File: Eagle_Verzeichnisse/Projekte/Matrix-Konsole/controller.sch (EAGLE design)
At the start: 14 parts, among them IC1 74HC165D, X2 MINI-USB-32005-201

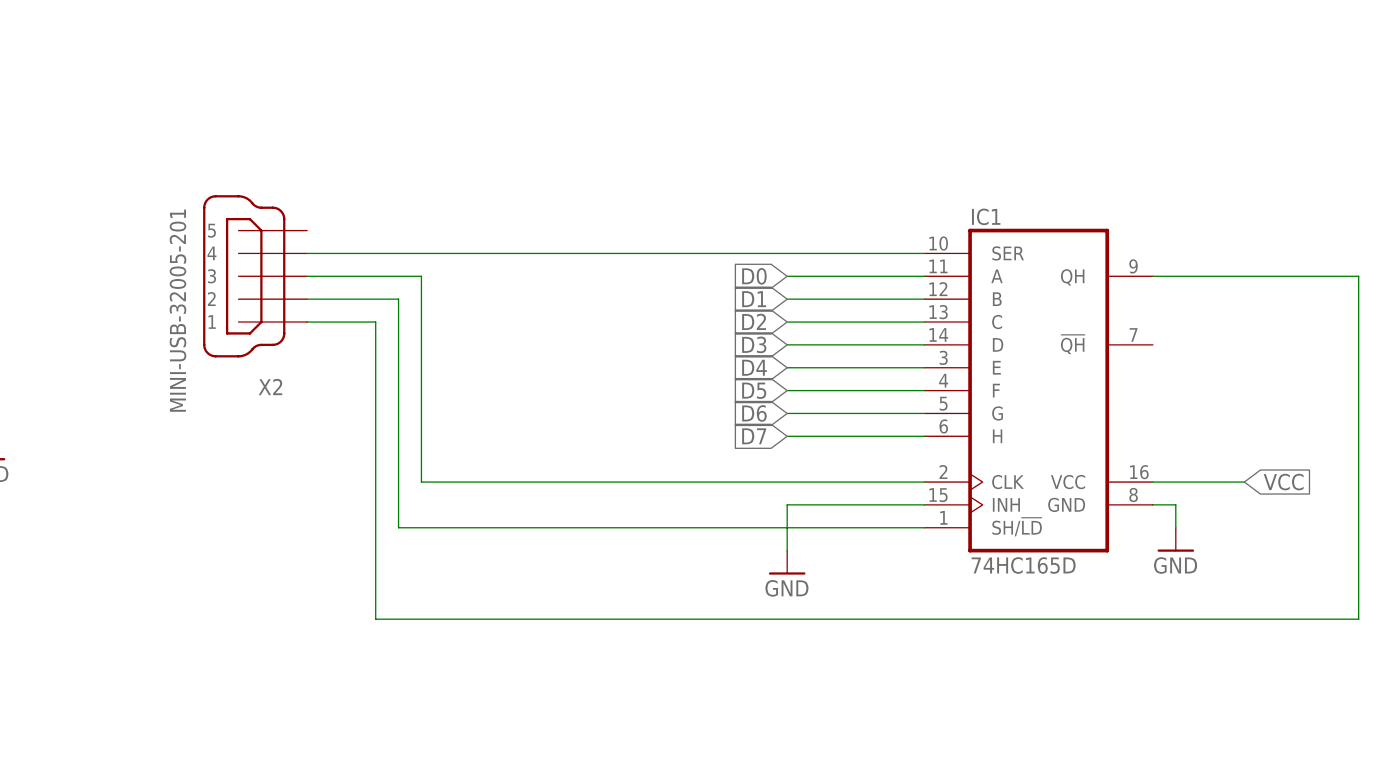
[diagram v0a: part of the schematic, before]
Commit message: Removed USB, Changed Labels
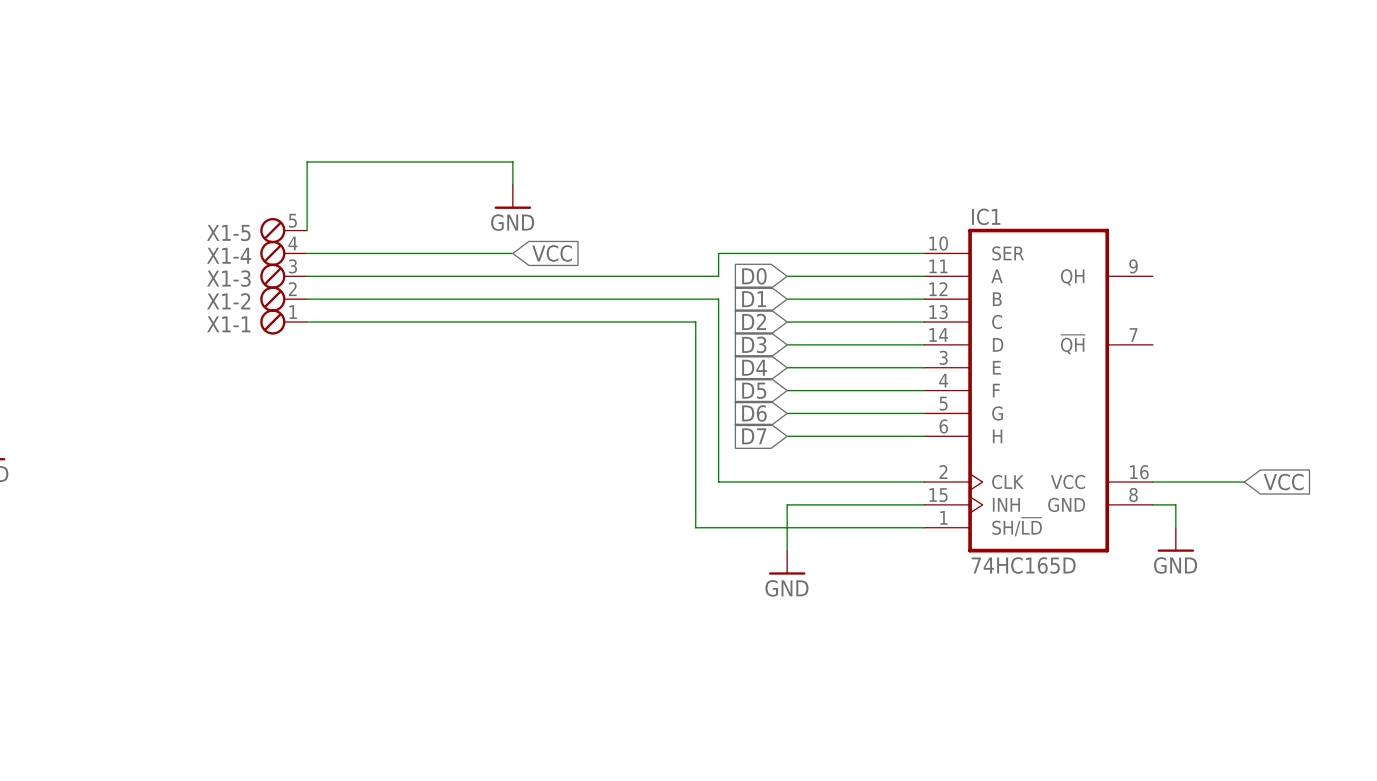
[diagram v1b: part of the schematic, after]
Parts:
- removed X2: MINI-USB-32005-201, con-cypressindustries:MINI-USB-32005-201
- added X1: (no value), con-phoenix-254:MPT5
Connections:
- removed net N$4: IC1.QH, X2.1
- net GND: now also X1-5.1
- net N$1: now also IC1.SH/!LD, X1-1.1; no longer IC1.SER, X2.4
- net N$2: now also X1-2.1; no longer X2.3
- net N$3: now also IC1.SER, X1-3.1; no longer IC1.SH/!LD, X2.2
- net VCC: now also X1-4.1
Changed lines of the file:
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@@
 <setting verticaltext="up"/>
 </settings>
-<grid distance="0.1" unitdist="inch" unit="inch" style="lines" multiple="1" display="no" altdistance="0.01" altunitdist="inch" altunit="inch"/>
+<grid distance="0.1" unitdist="inch" unit="inch" style="lines" multiple="1" display="yes" altdistance="0.01" altunitdist="inch" altunit="inch"/>
 <layers>
 <layer number="1" name="Top" color="4" fill="1" visible="no" active="no"/>
@@
 <part name="GND7" library="supply1" deviceset="GND" device=""/>
 <part name="GND8" library="supply1" deviceset="GND" device=""/>
-<part name="X2" library="con-cypressindustries" deviceset="MINI-USB-" device="32005-201"/>
+<part name="X1" library="con-phoenix-254" deviceset="MPT5" device=""/>
+<part name="GND9" library="supply1" deviceset="GND" device=""/>
 </parts>
 <sheets>
@@
 <instance part="GND7" gate="1" x="-86.36" y="-50.8"/>
 <instance part="GND8" gate="1" x="-5.08" y="22.86"/>
-<instance part="X2" gate="G$1" x="-63.5" y="55.88" rot="R180"/>
+<instance part="X1" gate="-1" x="-60.96" y="50.8" rot="R180"/>
+<instance part="X1" gate="-2" x="-60.96" y="53.34" rot="R180"/>
+<instance part="X1" gate="-3" x="-60.96" y="55.88" rot="R180"/>
+<instance part="X1" gate="-4" x="-60.96" y="58.42" rot="R180"/>
+<instance part="X1" gate="-5" x="-60.96" y="60.96" rot="R180"/>
+<instance part="GND9" gate="1" x="-35.56" y="63.5"/>
 </instances>
 <busses>
 </busses>
 <nets>
-<net name="N$1" class="0">
-<segment>
-<wire x1="10.16" y1="58.42" x2="-58.42" y2="58.42" width="0.1524" layer="91"/>
-<pinref part="IC1" gate="A" pin="SER"/>
-<pinref part="X2" gate="G$1" pin="4"/>
-</segment>
-</net>
-<net name="N$2" class="0">
-<segment>
-<wire x1="10.16" y1="33.02" x2="-45.72" y2="33.02" width="0.1524" layer="91"/>
-<wire x1="-45.72" y1="33.02" x2="-45.72" y2="55.88" width="0.1524" layer="91"/>
-<wire x1="-45.72" y1="55.88" x2="-58.42" y2="55.88" width="0.1524" layer="91"/>
-<pinref part="IC1" gate="A" pin="CLK"/>
-<pinref part="X2" gate="G$1" pin="3"/>
-</segment>
-</net>
-<net name="N$3" class="0">
-<segment>
-<wire x1="10.16" y1="27.94" x2="-48.26" y2="27.94" width="0.1524" layer="91"/>
-<wire x1="-48.26" y1="27.94" x2="-48.26" y2="53.34" width="0.1524" layer="91"/>
-<wire x1="-48.26" y1="53.34" x2="-58.42" y2="53.34" width="0.1524" layer="91"/>
-<pinref part="IC1" gate="A" pin="SH/!LD"/>
-<pinref part="X2" gate="G$1" pin="2"/>
-</segment>
-</net>
-<net name="N$4" class="0">
-<segment>
-<wire x1="35.56" y1="55.88" x2="58.42" y2="55.88" width="0.1524" layer="91"/>
-<wire x1="58.42" y1="55.88" x2="58.42" y2="17.78" width="0.1524" layer="91"/>
-<wire x1="58.42" y1="17.78" x2="-50.8" y2="17.78" width="0.1524" layer="91"/>
-<wire x1="-50.8" y1="17.78" x2="-50.8" y2="50.8" width="0.1524" layer="91"/>
-<wire x1="-50.8" y1="50.8" x2="-58.42" y2="50.8" width="0.1524" layer="91"/>
-<pinref part="IC1" gate="A" pin="QH"/>
-<pinref part="X2" gate="G$1" pin="1"/>
-</segment>
-</net>
 <net name="GND" class="0">
 <segment>
@@
 <pinref part="GND8" gate="1" pin="GND"/>
 </segment>
+<segment>
+<pinref part="X1" gate="-5" pin="1"/>
+<wire x1="-58.42" y1="60.96" x2="-58.42" y2="68.58" width="0.1524" layer="91"/>
+<wire x1="-58.42" y1="68.58" x2="-35.56" y2="68.58" width="0.1524" layer="91"/>
+<wire x1="-35.56" y1="68.58" x2="-35.56" y2="66.04" width="0.1524" layer="91"/>
+<pinref part="GND9" gate="1" pin="GND"/>
+</segment>
 </net>
 <net name="VCC" class="0">
@@
 <wire x1="-132.08" y1="-48.26" x2="-144.78" y2="-48.26" width="0.1524" layer="91"/>
 <label x="-144.78" y="-48.26" size="1.778" layer="95" rot="R180" xref="yes"/>
+</segment>
+<segment>
+<pinref part="X1" gate="-4" pin="1"/>
+<wire x1="-58.42" y1="58.42" x2="-35.56" y2="58.42" width="0.1524" layer="91"/>
+<label x="-35.56" y="58.42" size="1.778" layer="95" xref="yes"/>
 </segment>
 </net>
@@
 </segment>
 </net>
+<net name="N$1" class="0">
+<segment>
+<pinref part="IC1" gate="A" pin="SH/!LD"/>
+<wire x1="10.16" y1="27.94" x2="-15.24" y2="27.94" width="0.1524" layer="91"/>
+<wire x1="-15.24" y1="27.94" x2="-15.24" y2="50.8" width="0.1524" layer="91"/>
+<pinref part="X1" gate="-1" pin="1"/>
+<wire x1="-15.24" y1="50.8" x2="-58.42" y2="50.8" width="0.1524" layer="91"/>
+</segment>
+</net>
+<net name="N$2" class="0">
+<segment>
+<pinref part="IC1" gate="A" pin="CLK"/>
+<wire x1="10.16" y1="33.02" x2="-12.7" y2="33.02" width="0.1524" layer="91"/>
+<wire x1="-12.7" y1="33.02" x2="-12.7" y2="53.34" width="0.1524" layer="91"/>
+<pinref part="X1" gate="-2" pin="1"/>
+<wire x1="-12.7" y1="53.34" x2="-58.42" y2="53.34" width="0.1524" layer="91"/>
+</segment>
+</net>
+<net name="N$3" class="0">
+<segment>
+<pinref part="IC1" gate="A" pin="SER"/>
+<wire x1="10.16" y1="58.42" x2="-12.7" y2="58.42" width="0.1524" layer="91"/>
+<wire x1="-12.7" y1="58.42" x2="-12.7" y2="55.88" width="0.1524" layer="91"/>
+<pinref part="X1" gate="-3" pin="1"/>
+<wire x1="-12.7" y1="55.88" x2="-58.42" y2="55.88" width="0.1524" layer="91"/>
+</segment>
+</net>
